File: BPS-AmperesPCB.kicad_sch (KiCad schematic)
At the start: 26 parts, among them J1 Conn_01x04, J2 PeripheralCANConnector, J3 PeripheralCANConnector, U1 PeripheralSOM, U2 INA145UA/2K5, U3 AMC1300BDWV, U4 RO-123.3S_HP

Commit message: Testpoints and Math
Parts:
- added +12V, +3V3, +3V3High, ADC_In, GND, GNDHigh, GNDPWR, INN, INP, OUTN, OUTP, VOut: TestPoint, symbol Connector:TestPoint
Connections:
- net +12V: now also +12V.1
- net +3V3: now also +3V3.1
- net +3V3 High: now also +3V3High.1
- net ADC_In: now also ADC_In.1
- net GND: now also GND.1
- net GND High: now also GNDHigh.1
- net GNDPWR: now also GNDPWR.1
- net INN: now also INN.1
- net INP: now also INP.1
- net OUTN: now also OUTN.1
- net OUTP: now also OUTP.1
- net at D2.2 (A), D3.1 (K), R6.1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: now also VOut.1
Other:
- note added: "250 uOhm Shunt Resistor Between 1 and 2"
- note added: "Expected Range for Current: 0A - 120A"
- note added: "Input Voltage Range: 0V - 0.03V"
- note added: "Max Protected Current: 222A"
- note added: "Maximum Voltage Protected: -2.7V - 6V"
- note added: "Output Voltage Range: 0V - 0.25V"
- note added: "Output Voltage Range: 0V - 3.25V"
- note added: "Total Gain (V/A): 0.027"

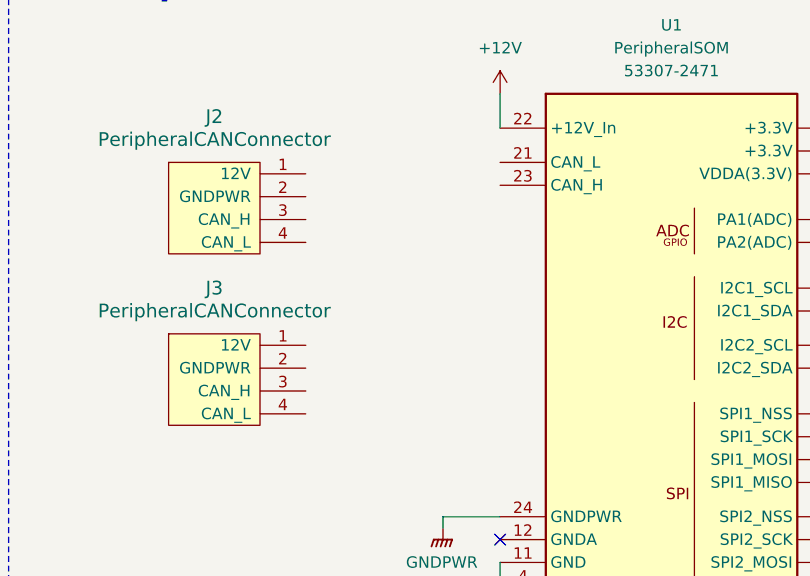
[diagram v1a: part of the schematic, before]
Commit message: Daisy Chain CAN Connectors
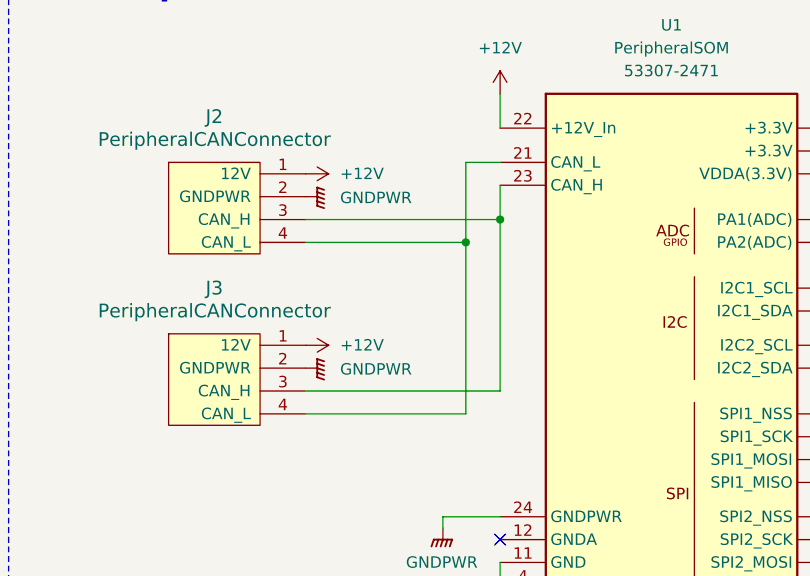
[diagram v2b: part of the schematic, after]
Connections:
- net +12V: now also J2.1 (12V), J3.1 (12V)
- net GNDPWR: now also J2.2 (GNDPWR), J3.2 (GNDPWR)
- net at J2.3 (CAN_H): now also J3.3 (CAN_H), U1.23 (CAN_H)
- net at J2.4 (CAN_L): now also J3.4 (CAN_L), U1.21 (CAN_L)
